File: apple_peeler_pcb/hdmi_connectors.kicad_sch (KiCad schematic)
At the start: 2 parts, among them J3 HYC10-HDMIA19-600B, J4 HYC10-HDMIA19-600B

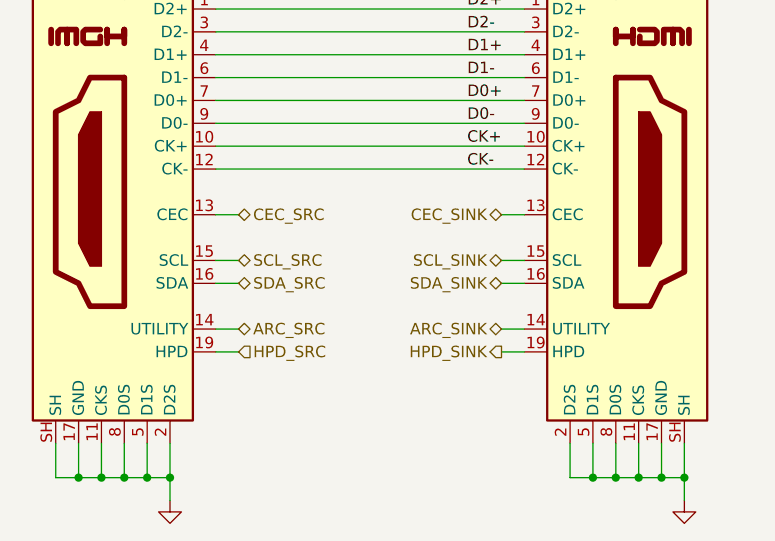
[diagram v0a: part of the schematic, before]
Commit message: rg | xargs sed goes brrr
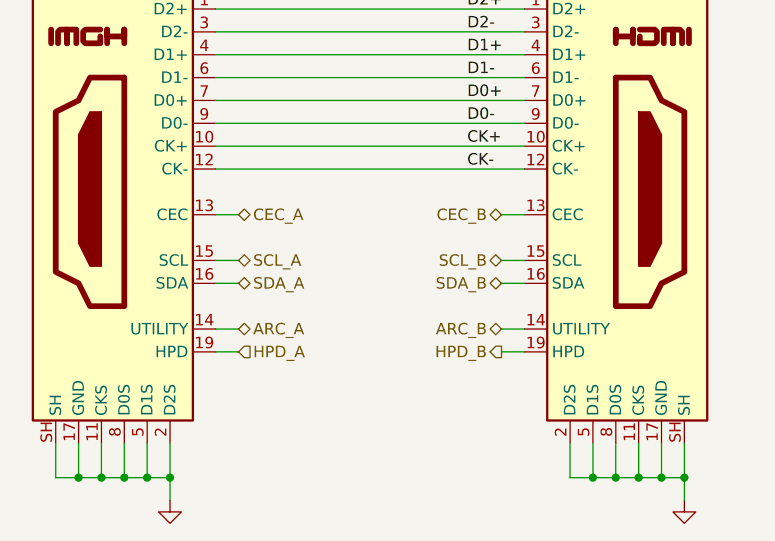
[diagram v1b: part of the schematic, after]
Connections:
- net ARC_SINK renamed ARC_B
- net ARC_SRC renamed ARC_A
- net CEC_SINK renamed CEC_B
- net CEC_SRC renamed CEC_A
- net HPD_SINK renamed HPD_B
- net HPD_SRC renamed HPD_A
- net SCL_SINK renamed SCL_B
- net SCL_SRC renamed SCL_A
- net SDA_SINK renamed SDA_B
- net SDA_SRC renamed SDA_A
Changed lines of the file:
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@@
 		)
 	)
-	(hierarchical_label "HPD_SINK"
+	(hierarchical_label "HPD_B"
 		(shape output)
 		(at 161.29 113.03 180)
@@
 		)
 	)
-	(hierarchical_label "ARC_SINK"
+	(hierarchical_label "ARC_B"
 		(shape bidirectional)
 		(at 161.29 110.49 180)
@@
 		)
 	)
-	(hierarchical_label "SDA_SRC"
+	(hierarchical_label "SDA_A"
 		(shape bidirectional)
 		(at 132.08 105.41 0)
@@
 		)
 	)
-	(hierarchical_label "HPD_SRC"
+	(hierarchical_label "HPD_A"
 		(shape input)
 		(at 132.08 113.03 0)
@@
 		)
 	)
-	(hierarchical_label "CEC_SINK"
+	(hierarchical_label "CEC_B"
 		(shape bidirectional)
 		(at 161.29 97.79 180)
@@
 		)
 	)
-	(hierarchical_label "CEC_SRC"
+	(hierarchical_label "CEC_A"
 		(shape bidirectional)
 		(at 132.08 97.79 0)
@@
 		)
 	)
-	(hierarchical_label "SDA_SINK"
+	(hierarchical_label "SDA_B"
 		(shape bidirectional)
 		(at 161.29 105.41 180)
@@
 		)
 	)
-	(hierarchical_label "ARC_SRC"
+	(hierarchical_label "ARC_A"
 		(shape bidirectional)
 		(at 132.08 110.49 0)
@@
 		)
 	)
-	(hierarchical_label "SCL_SINK"
+	(hierarchical_label "SCL_B"
 		(shape bidirectional)
 		(at 161.29 102.87 180)
@@
 		)
 	)
-	(hierarchical_label "SCL_SRC"
+	(hierarchical_label "SCL_A"
 		(shape bidirectional)
 		(at 132.08 102.87 0)

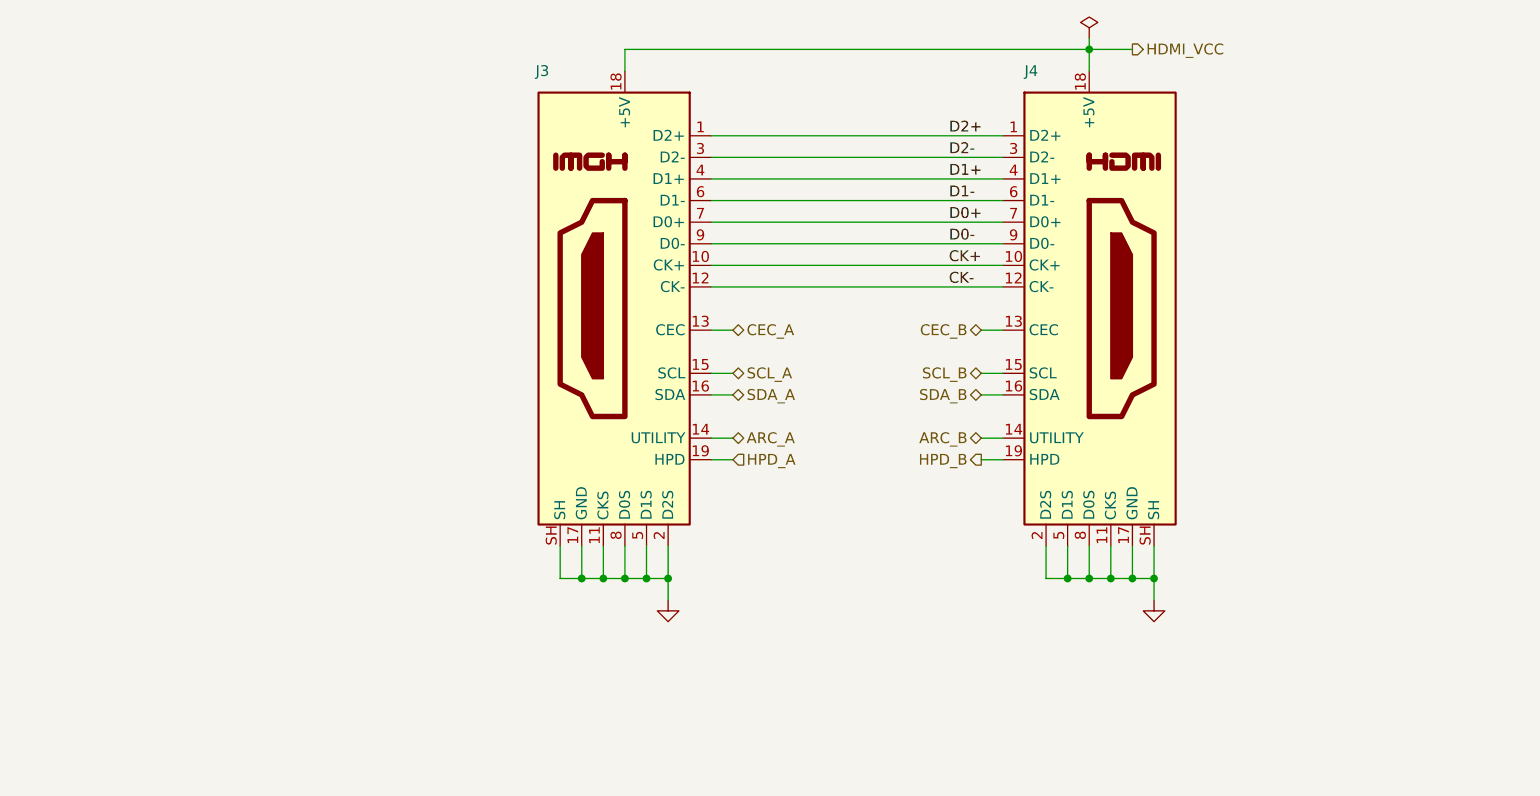
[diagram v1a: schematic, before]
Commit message: add loads of test points
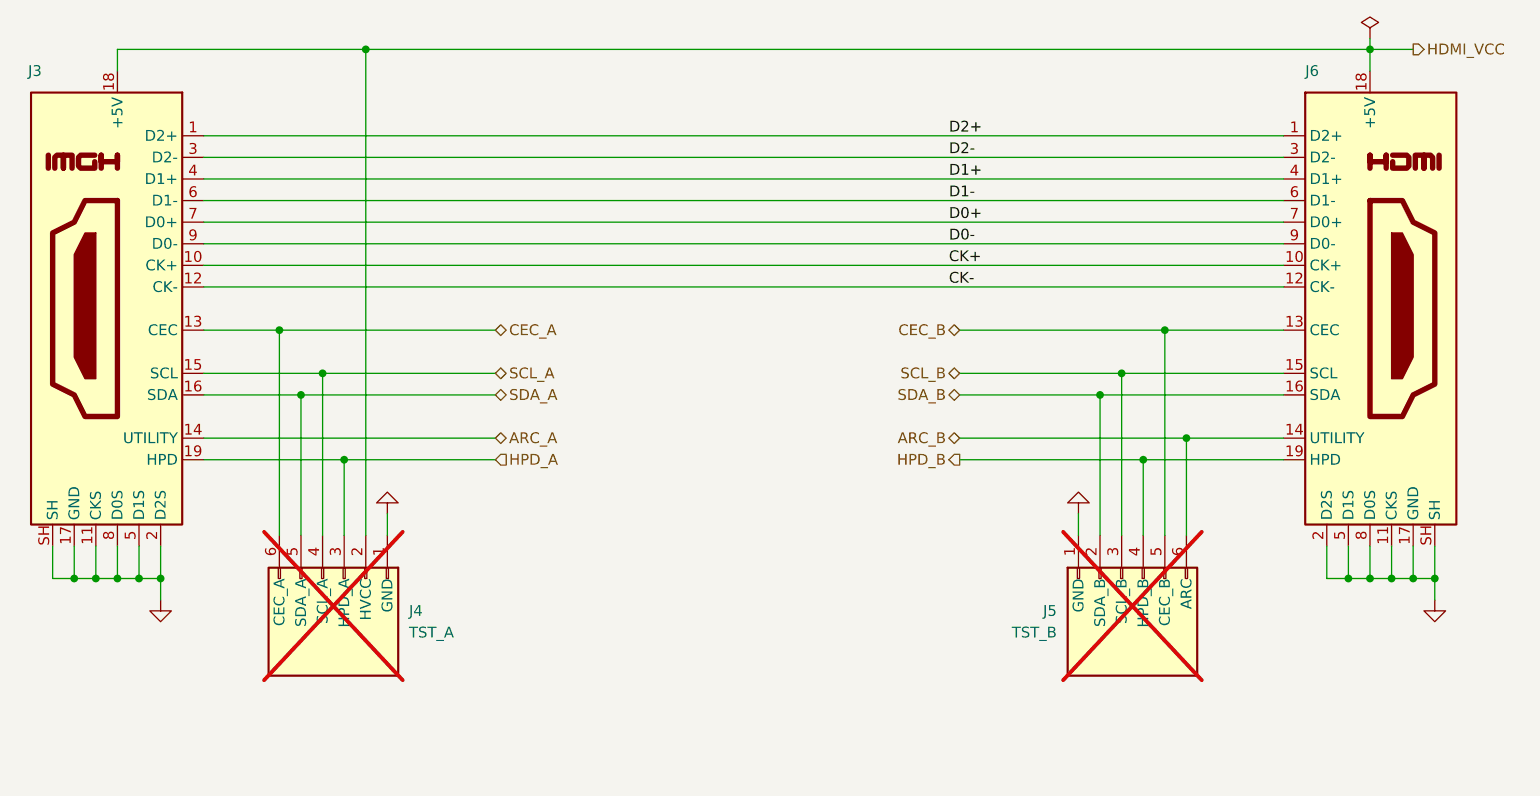
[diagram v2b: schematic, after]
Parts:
- added J4, J5: Header_01x06, conn:PinHeader_1x06_P2.54mm_Vertical, symbol conn:Conn_01x06
- renumbered J4 to J6
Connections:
- net ARC_B: now also J5.6 (Pin_6)
- net CEC_A: now also J4.6 (Pin_6)
- net CEC_B: now also J5.5 (Pin_5)
- net GND: now also J4.1 (Pin_1), J5.1 (Pin_1)
- net HDMI_VCC: now also J4.2 (Pin_2)
- net HPD_A: now also J4.3 (Pin_3)
- net HPD_B: now also J5.4 (Pin_4)
- net SCL_A: now also J4.4 (Pin_4)
- net SCL_B: now also J5.3 (Pin_3)
- net SDA_A: now also J4.5 (Pin_5)
- net SDA_B: now also J5.2 (Pin_2)
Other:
- moved on the sheet: J3, J6

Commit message: route all power traces
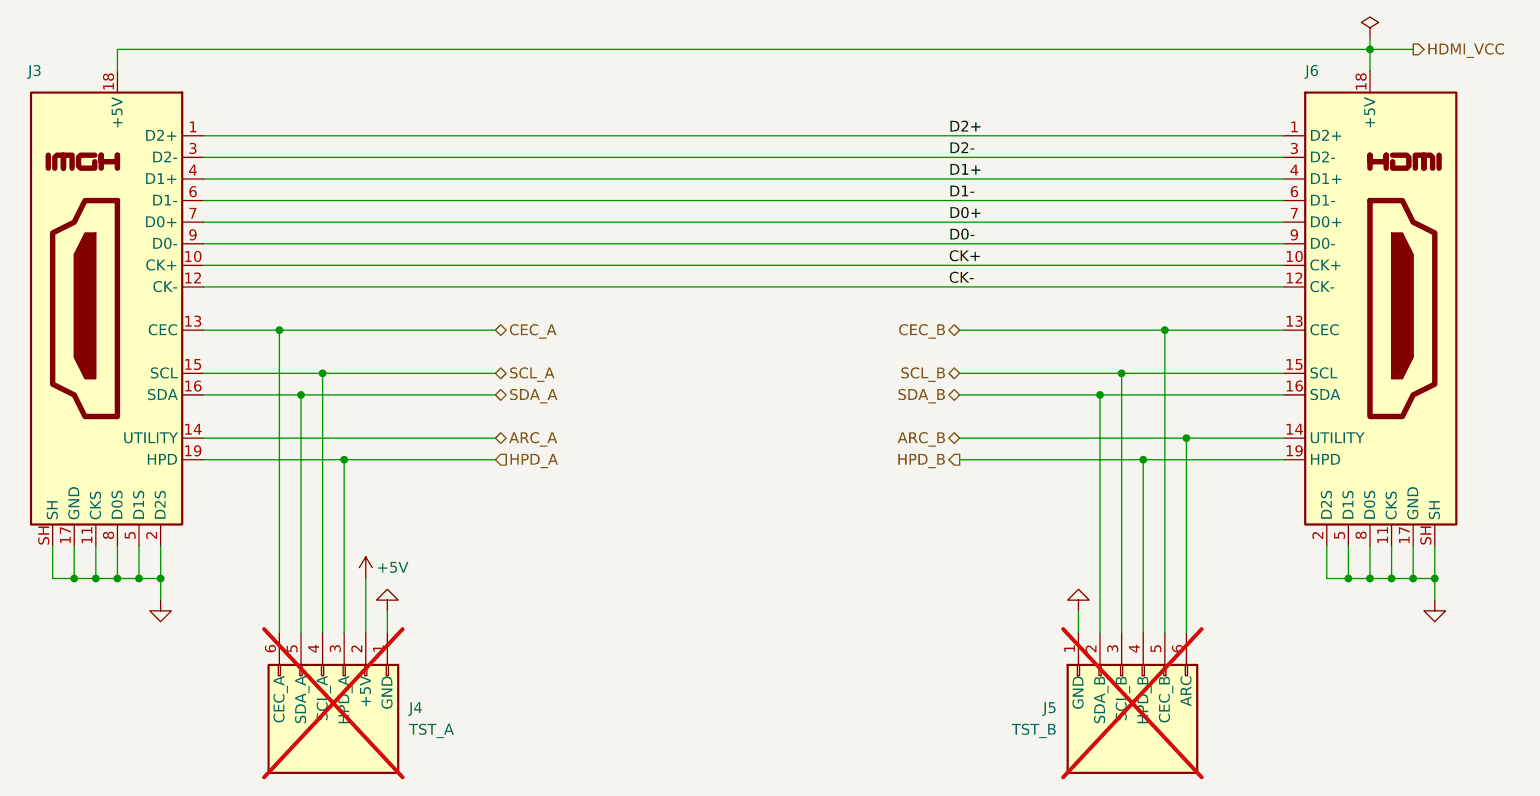
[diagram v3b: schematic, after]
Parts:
- J4: Purpose Pin3 HVCC -> +5V
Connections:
- net HDMI_VCC: no longer J4.2 (Pin_2)
- new net +5V: J4.2 (Pin_2)
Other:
- moved on the sheet: J4, J5

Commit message: fix connector labels and misc silkscreen
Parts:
- J4: Purpose Pin2 HPD_A -> +5V; Purpose Pin3 +5V -> HPD_A
- J5: Purpose Pin2 SCL_B -> SDA_B; Purpose Pin3 SDA_B -> SCL_B; Purpose Pin6 ARC -> P14
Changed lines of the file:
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@@
 		(dnp yes)
 		(property "Reference" "J5"
-			(at 170.18 142.2399 90)
-			(effects
-				(font
-					(size 1.27 1.27)
-				)
-				(justify left)
+			(at 170.18 138.43 0)
+			(effects
+				(font
+					(size 1.27 1.27)
+				)
 			)
 		)
@@
 			)
 		)
-		(property "Purpose Pin2" "SCL_B"
+		(property "Purpose Pin2" "SDA_B"
+			(at 175.26 138.43 0)
+			(do_not_autoplace yes)
+			(effects
+				(font
+					(size 1.27 1.27)
+				)
+				(justify left)
+			)
+		)
+		(property "Purpose Pin3" "SCL_B"
 			(at 177.8 138.43 0)
-			(do_not_autoplace yes)
-			(effects
-				(font
-					(size 1.27 1.27)
-				)
-				(justify left)
-			)
-		)
-		(property "Purpose Pin3" "SDA_B"
-			(at 175.26 138.43 0)
 			(do_not_autoplace yes)
 			(effects
@@
 			)
 		)
-		(property "Purpose Pin6" "ARC"
+		(property "Purpose Pin6" "P14"
 			(at 185.42 138.43 0)
 			(do_not_autoplace yes)
@@
 		)
 		(property "Purpose" "TST_B"
-			(at 170.18 144.7799 90)
-			(effects
-				(font
-					(size 1.27 1.27)
-				)
-				(justify left)
+			(at 170.18 146.05 0)
+			(effects
+				(font
+					(size 1.27 1.27)
+				)
 			)
 		)
@@
 		(dnp yes)
 		(property "Reference" "J4"
-			(at 93.98 142.2399 90)
-			(effects
-				(font
-					(size 1.27 1.27)
-				)
-				(justify left)
+			(at 93.98 138.43 0)
+			(effects
+				(font
+					(size 1.27 1.27)
+				)
 			)
 		)
@@
 			)
 		)
-		(property "Purpose Pin2" "HPD_A"
+		(property "Purpose Pin2" "+5V"
+			(at 88.9 138.43 0)
+			(do_not_autoplace yes)
+			(effects
+				(font
+					(size 1.27 1.27)
+				)
+				(justify left)
+			)
+		)
+		(property "Purpose Pin3" "HPD_A"
 			(at 86.36 138.43 0)
-			(do_not_autoplace yes)
-			(effects
-				(font
-					(size 1.27 1.27)
-				)
-				(justify left)
-			)
-		)
-		(property "Purpose Pin3" "+5V"
-			(at 88.9 138.43 0)
 			(do_not_autoplace yes)
 			(effects
@@
 		)
 		(property "Purpose" "TST_A"
-			(at 93.98 144.7799 90)
-			(effects
-				(font
-					(size 1.27 1.27)
-				)
-				(justify left)
-			)
-		)
+			(at 93.98 146.05 0)
+			(effects
+				(font
+					(size 1.27 1.27)
+				)
+			)
+		)

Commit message: change HDMI connector to one that's in stock
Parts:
- J3, J6: value HYC10-HDMIA19-600B -> HDMI-001 19PCBTP; LCSC C341098 -> C138388
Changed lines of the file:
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@@
 			)
 		)
-		(property "Value" "HYC10-HDMIA19-600B"
+		(property "Value" "HDMI-001 19PCBTP"
 			(at 194.31 135.89 0)
 			(effects
@@
 			)
 		)
-		(property "LCSC" "C341098"
+		(property "LCSC" "C138388"
 			(at 207.01 95.25 0)
 			(effects
@@
 			)
 		)
-		(property "Value" "HYC10-HDMIA19-600B"
+		(property "Value" "HDMI-001 19PCBTP"
 			(at 67.31 135.89 0)
 			(effects
@@
 			)
 		)
-		(property "LCSC" "C341098"
+		(property "LCSC" "C138388"
 			(at 59.69 95.25 0)
 			(effects

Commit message: replace fancy debug connectors by pin header to save $8
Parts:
- renumbered J3 to J2, J4 to J3, J5 to J4, J6 to J5
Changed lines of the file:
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@@
 		(on_board yes)
 		(dnp no)
-		(property "Reference" "J6"
+		(property "Reference" "J5"
 			(at 199.39 67.31 0)
 			(effects
@@
 			(project "apple_peeler_pcb"
 				(path "/d5946b96-44a8-4a28-8641-19803e1510af/ab4760da-4146-4688-a275-418314974b55/2fa9f3a3-becb-43b3-a84f-2d33edcebfa3"
-					(reference "J6")
+					(reference "J5")
 					(unit 1)
 				)
@@
 		(on_board yes)
 		(dnp no)
-		(property "Reference" "J3"
+		(property "Reference" "J2"
 			(at 50.8 67.31 0)
 			(effects
@@
 			(project "apple_peeler_pcb"
 				(path "/d5946b96-44a8-4a28-8641-19803e1510af/ab4760da-4146-4688-a275-418314974b55/2fa9f3a3-becb-43b3-a84f-2d33edcebfa3"
-					(reference "J3")
+					(reference "J2")
 					(unit 1)
 				)
@@
 		(on_board yes)
 		(dnp no)
-		(property "Reference" "#PWR021"
+		(property "Reference" "#PWR020"
 			(at 64.77 135.89 0)
 			(effects
@@
 			(project "apple_peeler_pcb"
 				(path "/d5946b96-44a8-4a28-8641-19803e1510af/ab4760da-4146-4688-a275-418314974b55/2fa9f3a3-becb-43b3-a84f-2d33edcebfa3"
-					(reference "#PWR021")
+					(reference "#PWR020")
 					(unit 1)
 				)
@@
 		(on_board yes)
 		(dnp no)
-		(property "Reference" "#PWR025"
+		(property "Reference" "#PWR024"
 			(at 214.63 135.89 0)
 			(effects
@@
 			(project "apple_peeler_pcb"
 				(path "/d5946b96-44a8-4a28-8641-19803e1510af/ab4760da-4146-4688-a275-418314974b55/2fa9f3a3-becb-43b3-a84f-2d33edcebfa3"
-					(reference "#PWR025")
+					(reference "#PWR024")
 					(unit 1)
 				)
@@
 		(on_board yes)
 		(dnp yes)
-		(property "Reference" "J5"
+		(property "Reference" "J4"
 			(at 170.18 138.43 0)
 			(effects
@@
 			(project "apple_peeler_pcb"
 				(path "/d5946b96-44a8-4a28-8641-19803e1510af/ab4760da-4146-4688-a275-418314974b55/2fa9f3a3-becb-43b3-a84f-2d33edcebfa3"
-					(reference "J5")
+					(reference "J4")
 					(unit 1)
 				)
@@
 		(on_board yes)
 		(dnp no)
-		(property "Reference" "#PWR024"
+		(property "Reference" "#PWR023"
 			(at 172.72 124.46 0)
 			(effects
@@
 			(project "apple_peeler_pcb"
 				(path "/d5946b96-44a8-4a28-8641-19803e1510af/ab4760da-4146-4688-a275-418314974b55/2fa9f3a3-becb-43b3-a84f-2d33edcebfa3"
-					(reference "#PWR024")
+					(reference "#PWR023")
 					(unit 1)
 				)
@@
 		(on_board yes)
 		(dnp no)
-		(property "Reference" "#PWR022"
+		(property "Reference" "#PWR021"
 			(at 88.9 130.81 0)
 			(effects
@@
 			(project "apple_peeler_pcb"
 				(path "/d5946b96-44a8-4a28-8641-19803e1510af/ab4760da-4146-4688-a275-418314974b55/2fa9f3a3-becb-43b3-a84f-2d33edcebfa3"
-					(reference "#PWR022")
+					(reference "#PWR021")
 					(unit 1)
 				)
@@
 		(on_board yes)
 		(dnp yes)
-		(property "Reference" "J4"
+		(property "Reference" "J3"
 			(at 93.98 138.43 0)
 			(effects
@@
 			(project "apple_peeler_pcb"
 				(path "/d5946b96-44a8-4a28-8641-19803e1510af/ab4760da-4146-4688-a275-418314974b55/2fa9f3a3-becb-43b3-a84f-2d33edcebfa3"
-					(reference "J4")
+					(reference "J3")
 					(unit 1)
 				)
@@
 		(on_board yes)
 		(dnp no)
-		(property "Reference" "#PWR023"
+		(property "Reference" "#PWR022"
 			(at 91.44 124.46 0)
 			(effects
@@
 			(project "apple_peeler_pcb"
 				(path "/d5946b96-44a8-4a28-8641-19803e1510af/ab4760da-4146-4688-a275-418314974b55/2fa9f3a3-becb-43b3-a84f-2d33edcebfa3"
-					(reference "#PWR023")
+					(reference "#PWR022")
 					(unit 1)
 				)
